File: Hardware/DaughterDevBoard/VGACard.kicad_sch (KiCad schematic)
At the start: 31 parts, among them J13 BANKA, J14 BANKB, J15 BANKD, J16 BANKC, J17 VGA_OUT, U3 SN74LVC2T45QDCURQ1, U4 SN74LVC2T45QDCURQ1, U5 SN74LVC2T45QDCURQ1, U6 SN74LVC8T245DBQR, U7 SN74LVC8T245DBQR, U8 SN74LVC8T245DBQR

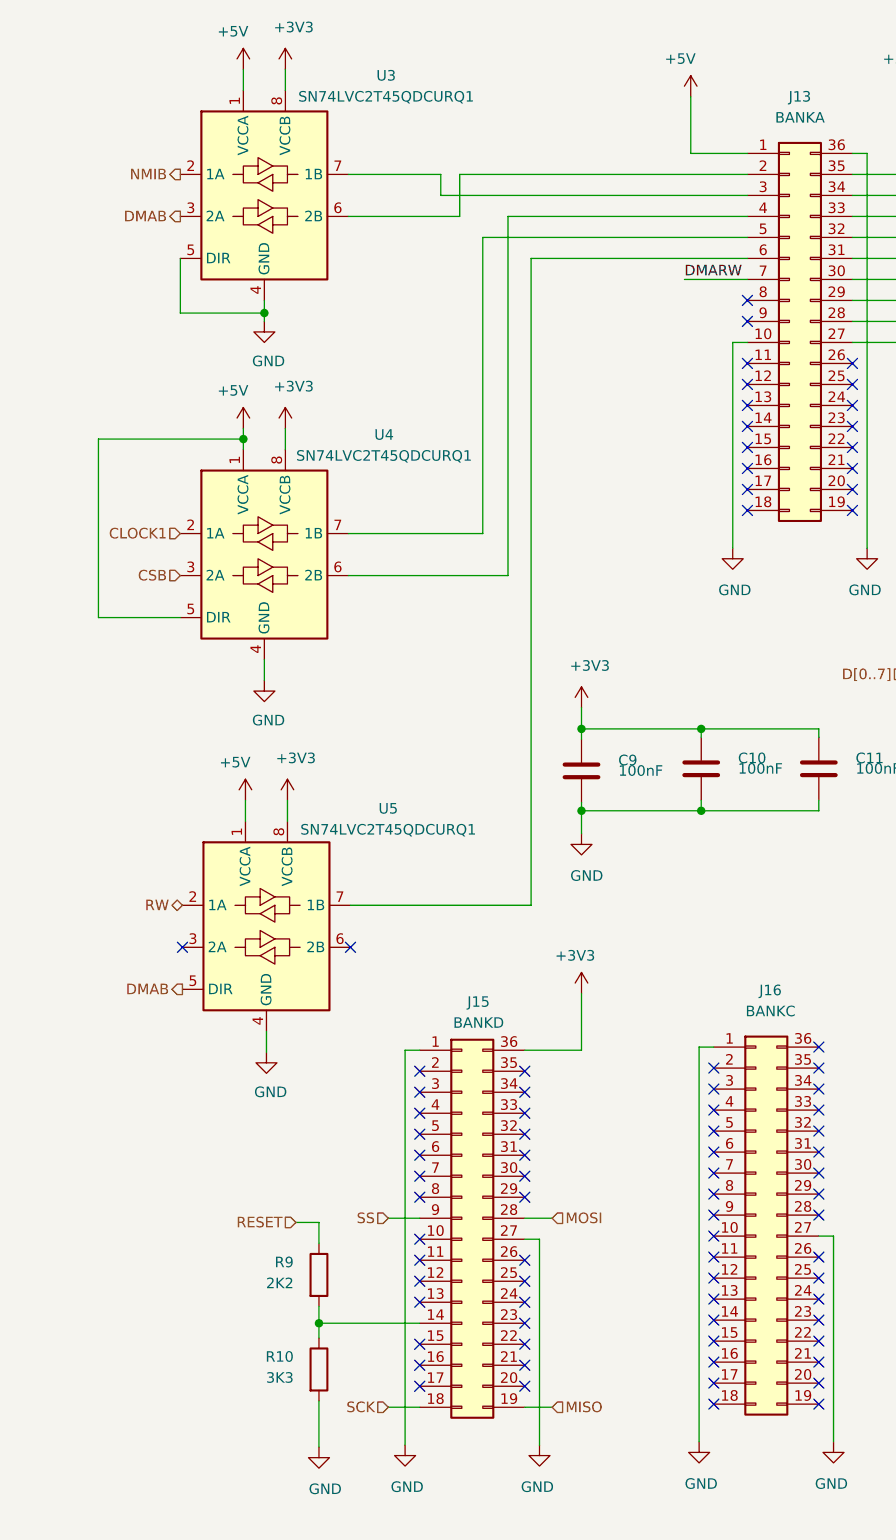
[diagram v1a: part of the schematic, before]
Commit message: Fix Reset, WAI Signal, Add PROG jumper and reformat luc files
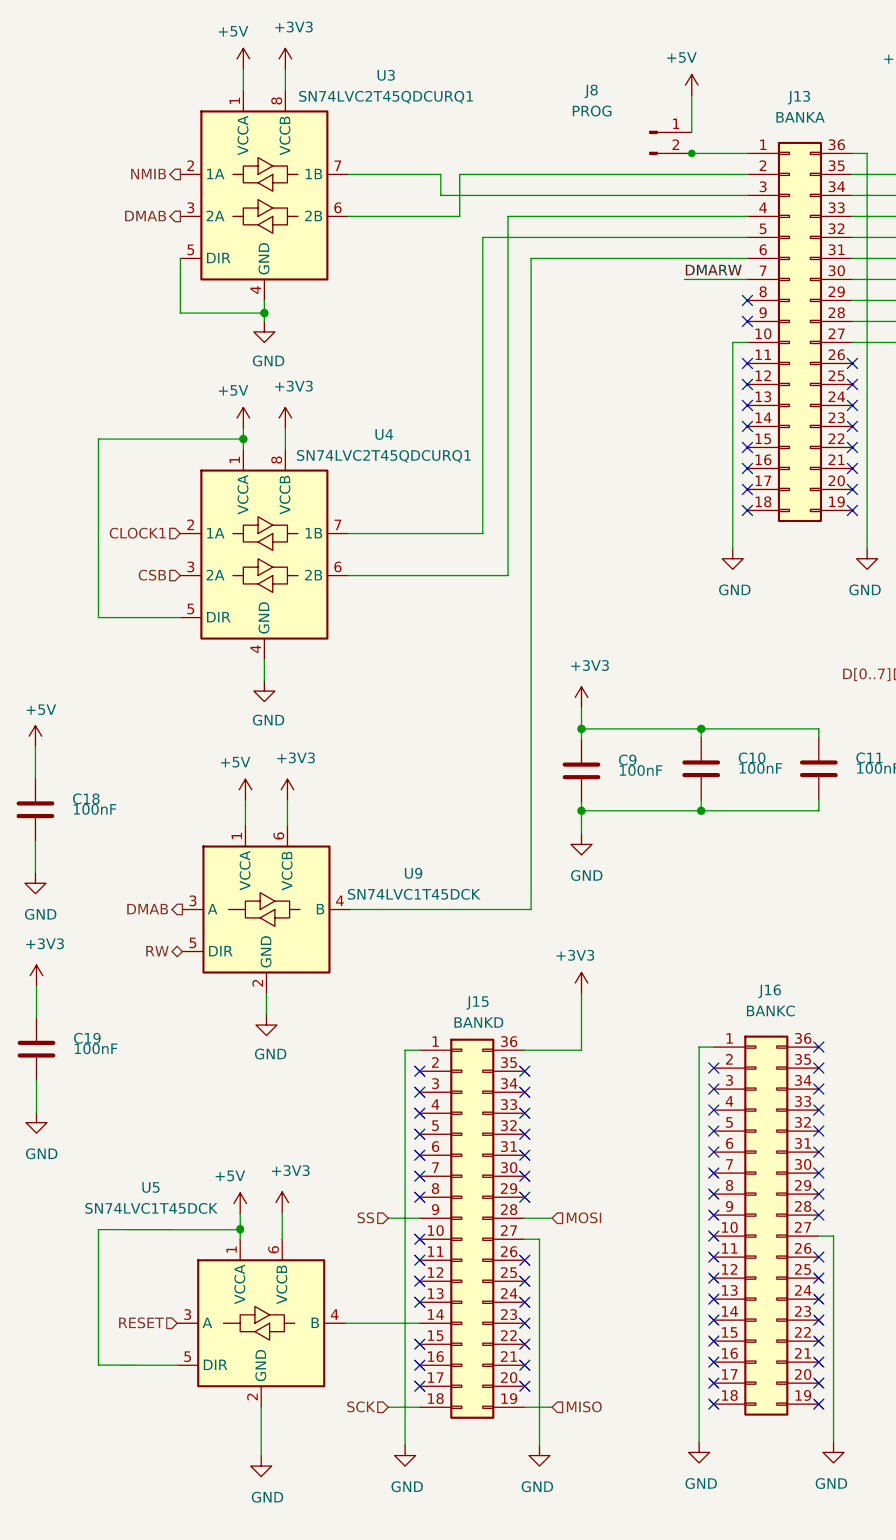
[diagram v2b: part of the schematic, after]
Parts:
- removed R10: 3K3, Resistor_THT:R_Axial_DIN0207_L6.3mm_D2.5mm_P10.16mm_Horizontal, symbol Device:R
- removed R9: 2K2, Resistor_THT:R_Axial_DIN0207_L6.3mm_D2.5mm_P10.16mm_Horizontal, symbol Device:R
- removed U5: SN74LVC2T45QDCURQ1, Package_SO:VSSOP-8_2.3x2mm_P0.5mm, symbol Logic_LevelTranslator:74LVC2T45DC
- added C18, C19: 100nF, Capacitor_SMD:C_0603_1608Metric, symbol Device:C
- added J8: PROG, Connector_PinHeader_2.54mm:PinHeader_1x02_P2.54mm_Vertical, symbol Connector:Conn_01x02_Male
- added U5, U9: SN74LVC1T45DCK, Package_TO_SOT_SMD:SOT-363_SC-70-6, symbol Logic_LevelTranslator:SN74LVC1T45DCK
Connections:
- net +3V3: now also C19.1, U5.6 (VCCB), U9.6 (VCCB)
- net +5V: now also C18.1, J8.1 (Pin_1), U5.1 (VCCA), U5.5 (DIR), U9.1 (VCCA); no longer J13.1 (Pin_1)
- net DMAB: now also U9.3 (A)
- net GND: now also C18.2, C19.2, U5.2 (GND), U9.2 (GND)
- net RESET: now also U5.3 (A)
- net RW: now also U9.5 (DIR)
- net at J13.6 (Pin_6): now also U9.4 (B)
- net at J15.14 (Pin_14): now also U5.4 (B)
- new net: J13.1 (Pin_1), J8.2 (Pin_2)
- no-connect marks 98 -> 96

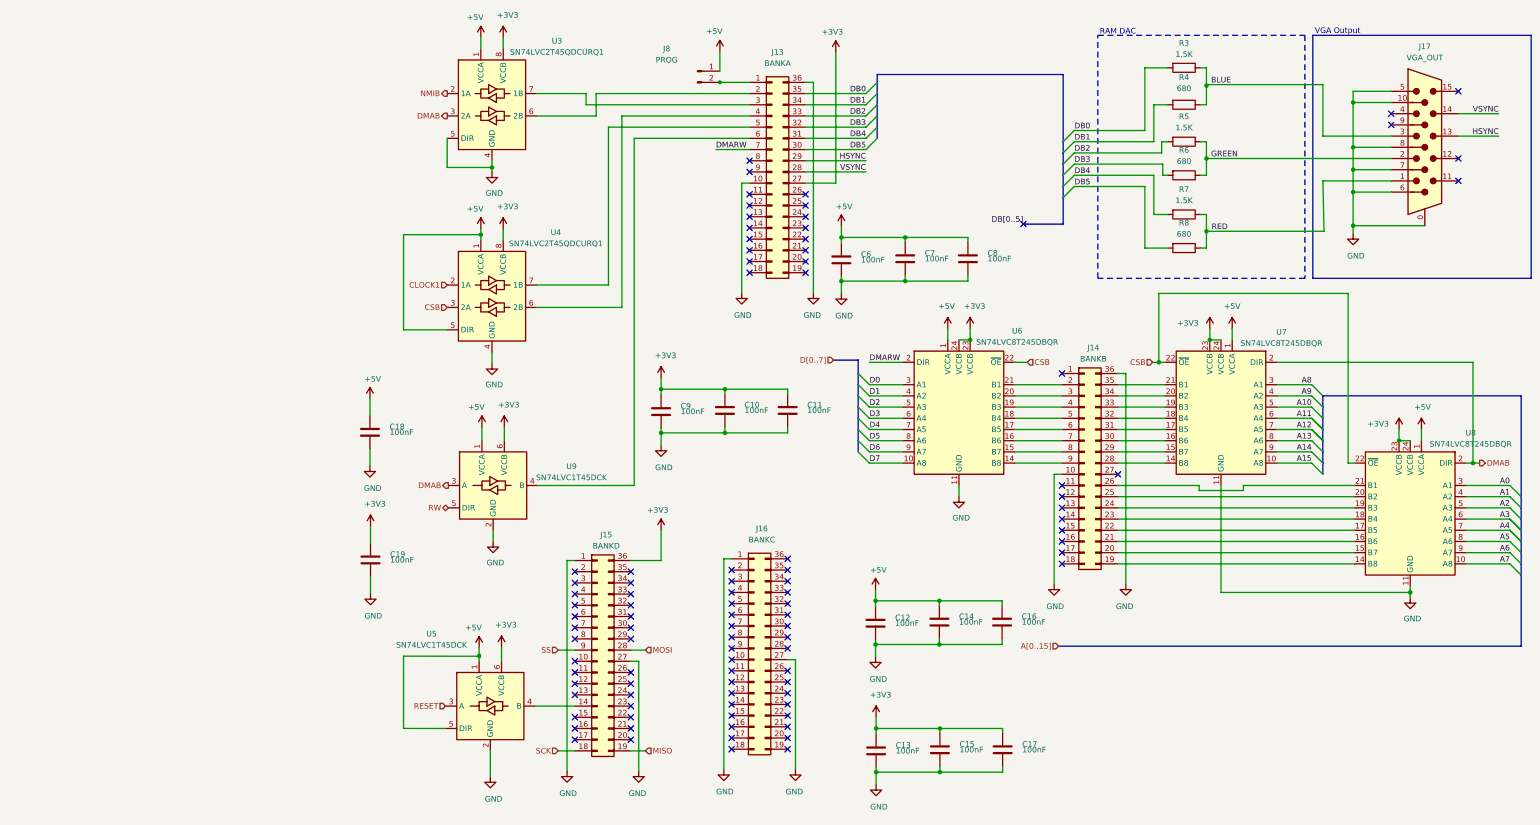
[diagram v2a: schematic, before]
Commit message: Add monostable to reset PPU
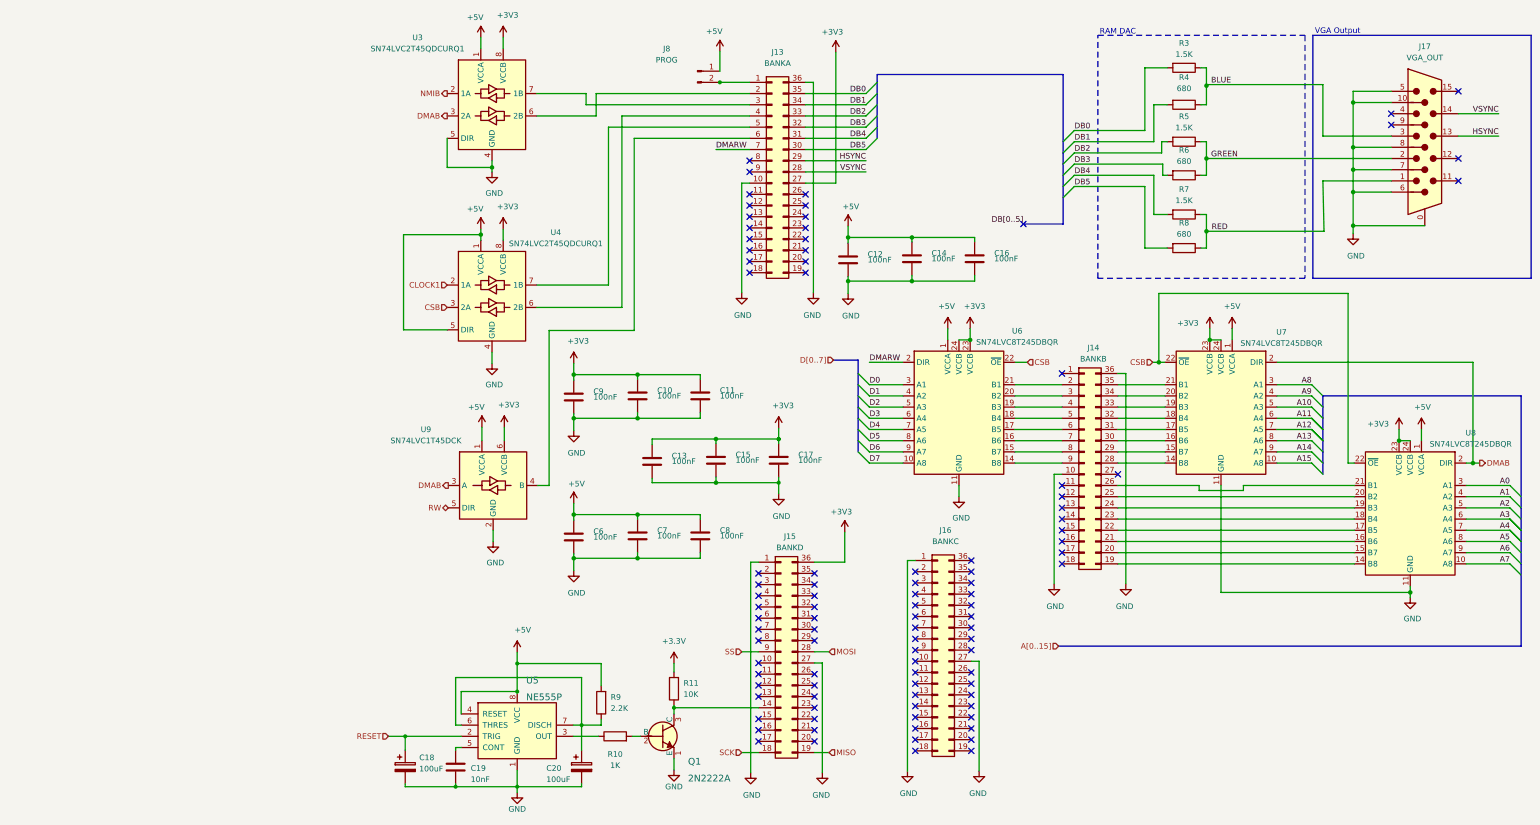
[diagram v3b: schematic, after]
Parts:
- removed C18: 100nF, Capacitor_SMD:C_0603_1608Metric, symbol Device:C
- removed U5: SN74LVC1T45DCK, Package_TO_SOT_SMD:SOT-363_SC-70-6, symbol Logic_LevelTranslator:SN74LVC1T45DCK
- added C18, C20: 100uF, symbol Device:C_Polarized
- added Q1: 2N2222A, digikey-footprints:TO-18-3, symbol dk_Transistors-Bipolar-BJT-Single:2N2222A
- added R10: 1K, Resistor_THT:R_Axial_DIN0207_L6.3mm_D2.5mm_P10.16mm_Horizontal, symbol Device:R
- added R11: 10K, Resistor_THT:R_Axial_DIN0207_L6.3mm_D2.5mm_P10.16mm_Horizontal, symbol Device:R
- added R9: 2.2K, Resistor_THT:R_Axial_DIN0207_L6.3mm_D2.5mm_P10.16mm_Horizontal, symbol Device:R
- added U5: NE555P, digikey-footprints:DIP-8_W7.62mm, symbol dk_Clock-Timing-Programmable-Timers-and-Oscillators:NE555P
- C19: value 100nF -> 10nF; footprint Capacitor_SMD:C_0603_1608Metric -> Capacitor_THT:C_Disc_D5.0mm_W2.5mm_P2.50mm
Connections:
- net +3V3: now also R11.2; no longer C19.1
- net +5V: now also R9.2, U5.4 (RESET), U5.8 (VCC)
- net GND: now also C18.2, C20.2, Q1.1 (E), U5.1 (GND)
- net RESET: now also C18.1, U5.2 (TRIG)
- net at J15.14 (Pin_14): now also Q1.3 (C), R11.1
- new net: R10.1, U5.3 (OUT)
- new net: Q1.2 (B), R10.2
- new net: C20.1, R9.1, U5.6 (THRES), U5.7 (DISCH)
- new net: C19.1, U5.5 (CONT)
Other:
- moved on the sheet: C10, C11, C12, C13, C14, C15, C16, C17, C6, C7, C8, C9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

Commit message: Cleanup
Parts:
- C18, C20: footprint (none) -> Capacitor_THT:CP_Radial_D5.0mm_P2.50mm
- Q1: footprint digikey-footprints:TO-18-3 -> Package_TO_SOT_THT:TO-18-3
- U5: footprint digikey-footprints:DIP-8_W7.62mm -> Package_DIP:DIP-8_W7.62mm
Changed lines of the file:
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@@
   )
   (symbol (lib_id "Device:R") (at 73.406 178.816 90) (unit 1)
-    (in_bom yes) (on_board yes) (fields_autoplaced)
-    (property "Reference" "R10" (id 0) (at 73.406 182.88 90))
-    (property "Value" "1K" (id 1) (at 73.406 185.42 90))
+    (in_bom yes) (on_board yes)
+    (property "Reference" "R10" (id 0) (at 73.66 181.61 90))
+    (property "Value" "1K" (id 1) (at 73.66 184.15 90))
     (property "Footprint" "Resistor_THT:R_Axial_DIN0207_L6.3mm_D2.5mm_P10.16mm_Horizontal" (id 2) (at 73.406 180.594 90)
       (effects (font (size 1.27 1.27)) hide)
@@
   (symbol (lib_id "Device:C_Polarized") (at 25.781 185.801 0) (unit 1)
     (in_bom yes) (on_board yes) (fields_autoplaced)
-    (property "Reference" "C18" (id 0) (at 28.956 183.6419 0)
-      (effects (font (size 1.27 1.27)) (justify left))
-    )
-    (property "Value" "100uF" (id 1) (at 28.956 186.1819 0)
-      (effects (font (size 1.27 1.27)) (justify left))
-    )
-    (property "Footprint" "" (id 2) (at 26.7462 189.611 0)
+    (property "Reference" "C18" (id 0) (at 29.21 183.6419 0)
+      (effects (font (size 1.27 1.27)) (justify left))
+    )
+    (property "Value" "100uF" (id 1) (at 29.21 186.1819 0)
+      (effects (font (size 1.27 1.27)) (justify left))
+    )
+    (property "Footprint" "Capacitor_THT:CP_Radial_D5.0mm_P2.50mm" (id 2) (at 26.7462 189.611 0)
       (effects (font (size 1.27 1.27)) hide)
     )
@@
   (symbol (lib_id "dk_Transistors-Bipolar-BJT-Single:2N2222A") (at 84.201 178.816 0) (unit 1)
     (in_bom yes) (on_board yes) (fields_autoplaced)
-    (property "Reference" "Q1" (id 0) (at 89.916 184.531 0)
+    (property "Reference" "Q1" (id 0) (at 88.9 177.546 0)
       (effects (font (size 1.524 1.524)) (justify left))
     )
-    (property "Value" "2N2222A" (id 1) (at 89.916 188.341 0)
+    (property "Value" "2N2222A" (id 1) (at 88.9 181.356 0)
       (effects (font (size 1.524 1.524)) (justify left))
     )
-    (property "Footprint" "digikey-footprints:TO-18-3" (id 2) (at 89.281 173.736 0)
+    (property "Footprint" "Package_TO_SOT_THT:TO-18-3" (id 2) (at 89.281 173.736 0)
       (effects (font (size 1.524 1.524)) (justify left) hide)
     )
@@
   )
   (symbol (lib_id "Device:C_Polarized") (at 65.786 185.801 0) (unit 1)
-    (in_bom yes) (on_board yes) (fields_autoplaced)
-    (property "Reference" "C20" (id 0) (at 57.785 186.055 0)
-      (effects (font (size 1.27 1.27)) (justify left))
-    )
-    (property "Value" "100uF" (id 1) (at 57.785 188.595 0)
-      (effects (font (size 1.27 1.27)) (justify left))
-    )
-    (property "Footprint" "" (id 2) (at 66.7512 189.611 0)
+    (in_bom yes) (on_board yes)
+    (property "Reference" "C20" (id 0) (at 67.31 188.595 0)
+      (effects (font (size 1.27 1.27)) (justify left))
+    )
+    (property "Value" "100uF" (id 1) (at 67.31 191.135 0)
+      (effects (font (size 1.27 1.27)) (justify left))
+    )
+    (property "Footprint" "Capacitor_THT:CP_Radial_D5.0mm_P2.50mm" (id 2) (at 66.7512 189.611 0)
       (effects (font (size 1.27 1.27)) hide)
     )
@@
   (symbol (lib_id "dk_Clock-Timing-Programmable-Timers-and-Oscillators:NE555P") (at 51.181 176.276 0) (unit 1)
     (in_bom yes) (on_board yes) (fields_autoplaced)
-    (property "Reference" "U5" (id 0) (at 53.2004 166.116 0)
+    (property "Reference" "U5" (id 0) (at 53.2004 165.1 0)
       (effects (font (size 1.524 1.524)) (justify left))
     )
-    (property "Value" "NE555P" (id 1) (at 53.2004 169.926 0)
+    (property "Value" "NE555P" (id 1) (at 53.2004 168.91 0)
       (effects (font (size 1.524 1.524)) (justify left))
     )
-    (property "Footprint" "digikey-footprints:DIP-8_W7.62mm" (id 2) (at 56.261 171.196 0)
-      (effects (font (size 1.524 1.524)) (justify left) hide)
-    )
+    (property "Footprint" "Package_DIP:DIP-8_W7.62mm" (id 2) (at 56.261 171.196 0)
+      (effects (font (size 1.524 1.524)) (justify left) hide)
+    )

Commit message: Fix
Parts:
- added J19: BANK_A, 4UCON:4UCON_2x25_P0.50mm_Vertical, symbol Connector_Generic:Conn_02x25_Counter_Clockwise
- added J20: BANK_C, 4UCON:4UCON_2x25_P0.50mm_Vertical, symbol Connector_Generic:Conn_02x25_Counter_Clockwise
- added J21: BANK_B, 4UCON:4UCON_2x25_P0.50mm_Vertical, symbol Connector_Generic:Conn_02x25_Counter_Clockwise
- added J22: BANK_D, 4UCON:4UCON_2x25_P0.50mm_Vertical, symbol Connector_Generic:Conn_02x25_Counter_Clockwise
